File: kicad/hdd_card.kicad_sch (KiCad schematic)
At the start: 17 parts, among them J1 POISK, J2 Conn_01x06, J3 Conn_01x06, U1 28C256, U2 74LS245, U3 28C256, U4 PIC18F47Q10-xP, U5 74LS38, U6 74LS32, U7 74LS74

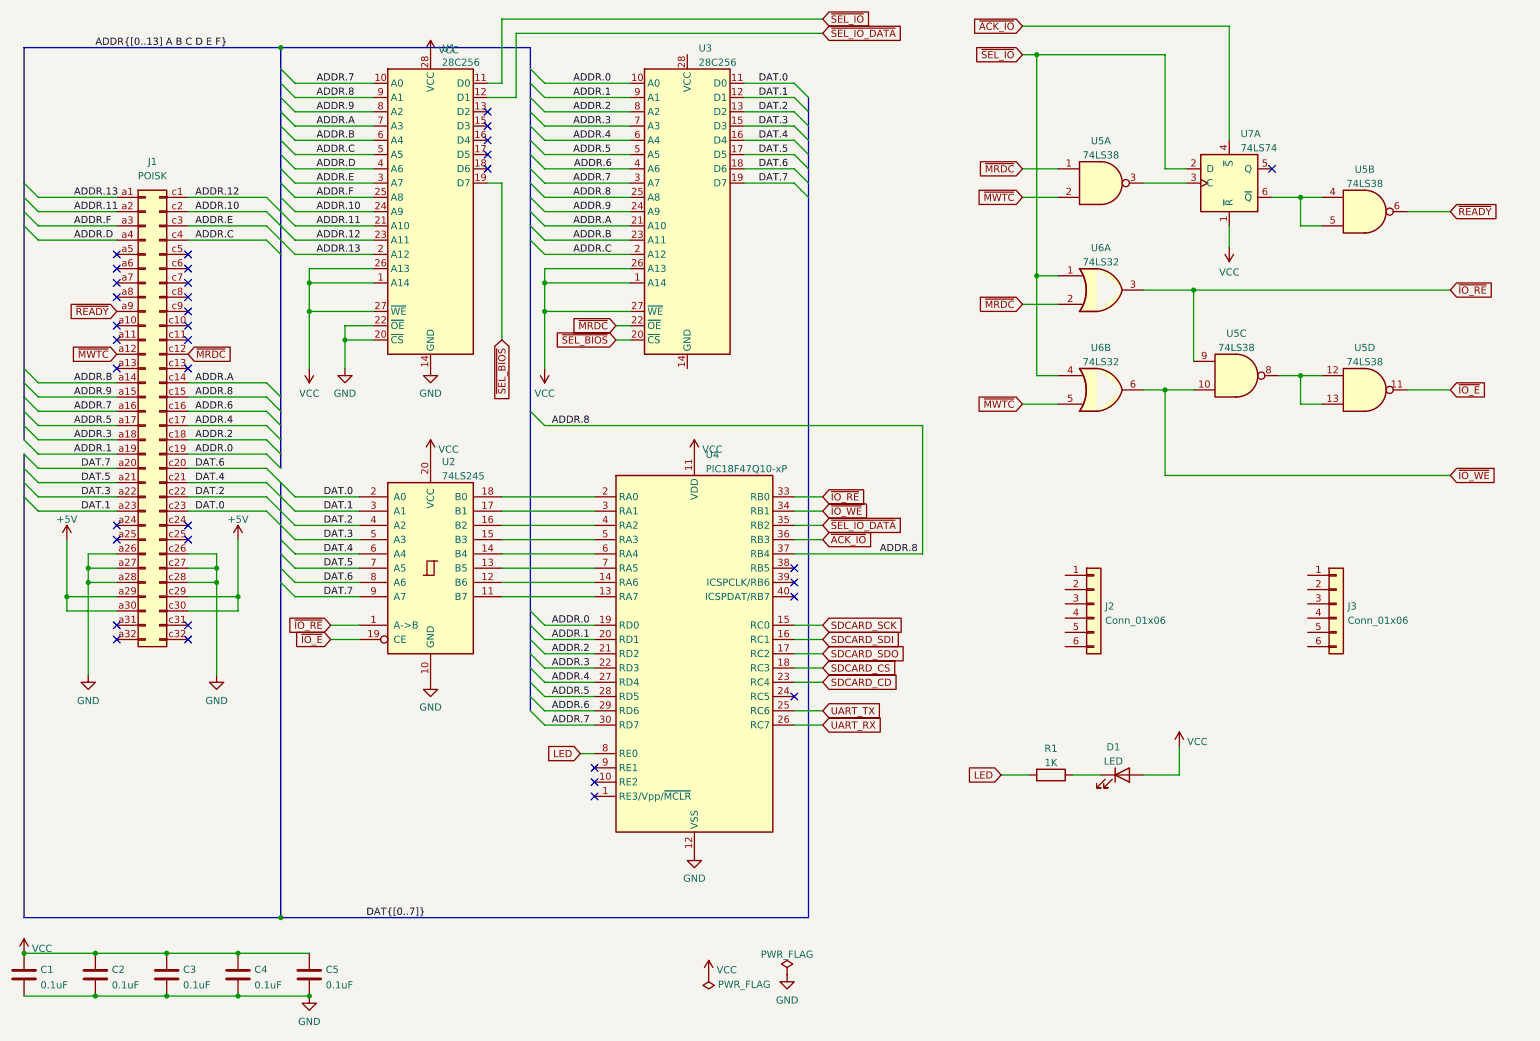
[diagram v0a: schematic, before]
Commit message: Connectors in schematic
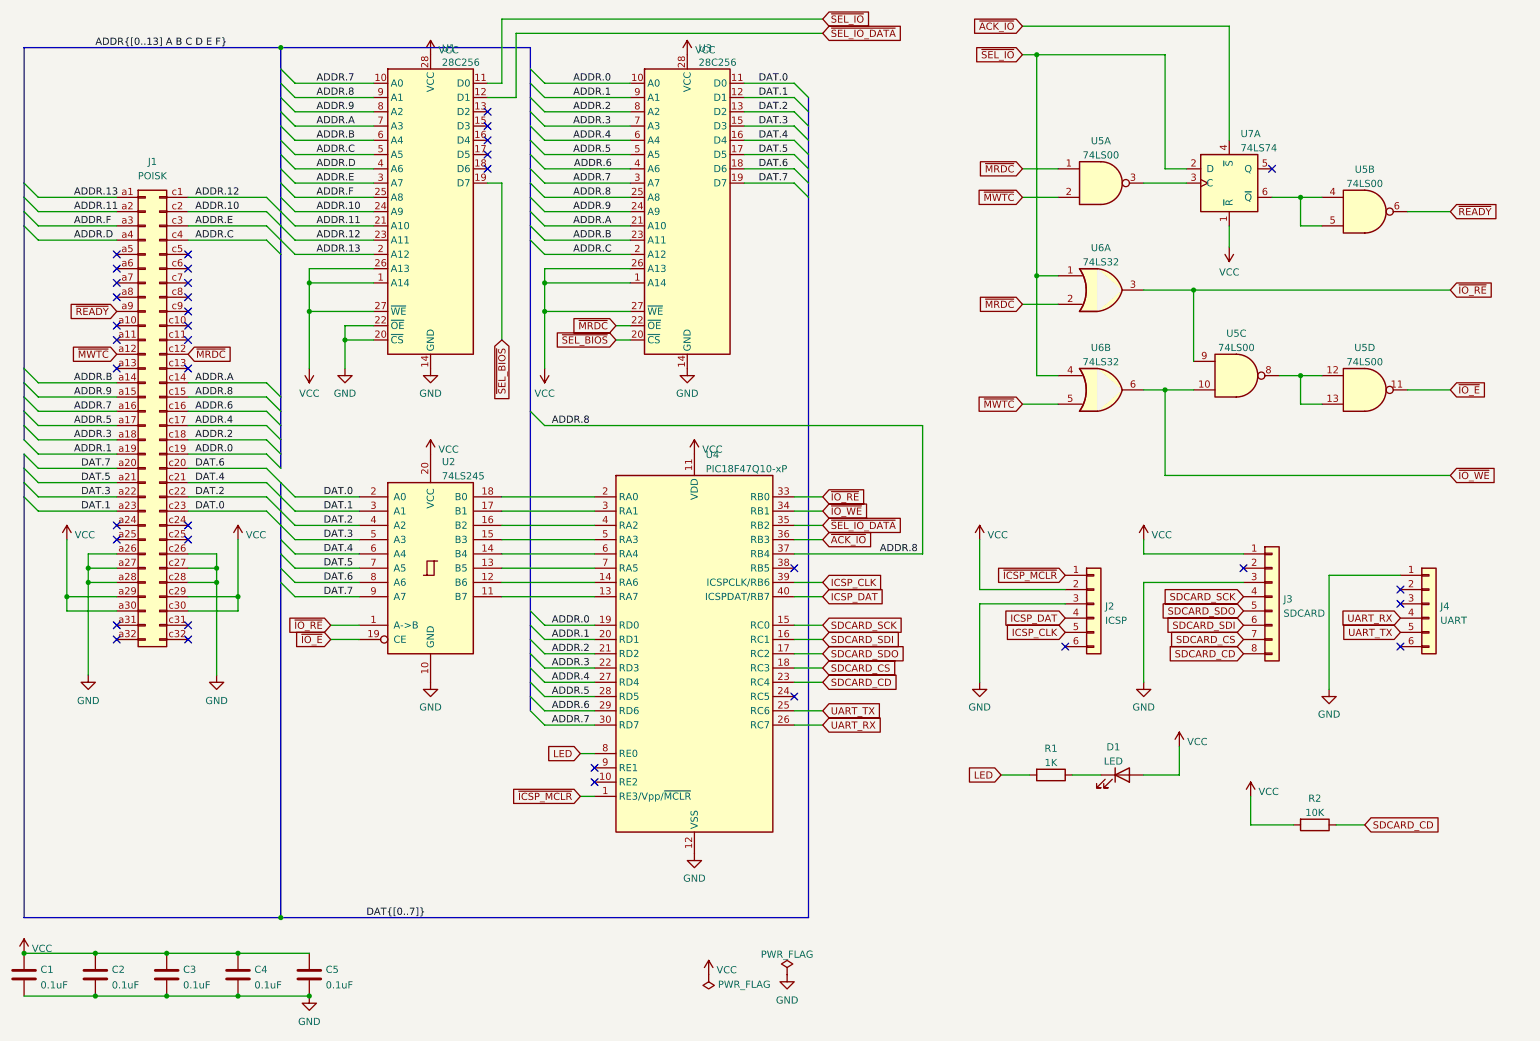
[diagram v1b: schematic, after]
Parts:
- removed U5: 74LS38, symbol 74xx:74LS38
- added J4: UART, symbol Connector_Generic:Conn_01x06
- added R2: 10K, symbol Device:R
- added U5: 74LS00, symbol 74xx:74LS00
- J2: value Conn_01x06 -> ICSP
- J3: value Conn_01x06 -> SDCARD; symbol Connector_Generic:Conn_01x06 -> Connector_Generic:Conn_01x08
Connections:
- net +5V is gone; now on net VCC: J1.a29 (Pin_a29), J1.a30 (Pin_a30), J1.c29 (Pin_c29), J1.c30 (Pin_c30)
- net GND: now also J2.3 (Pin_3), J3.3 (Pin_3), U3.14 (GND), J4.1 (Pin_1)
- net SDCARD_CD: now also J3.8 (Pin_8), R2.1
- net SDCARD_CS: now also J3.7 (Pin_7)
- net SDCARD_SCK: now also J3.4 (Pin_4)
- net SDCARD_SDI: now also J3.6 (Pin_6)
- net SDCARD_SDO: now also J3.5 (Pin_5)
- net UART_RX: now also J4.4 (Pin_4)
- net UART_TX: now also J4.5 (Pin_5)
- net VCC: now also J2.2 (Pin_2), J3.1 (Pin_1), U3.28 (VCC), R2.2
- net ~{IO_E}: now also U5.11
- net ~{IO_RE}: now also U5.9
- net ~{IO_WE}: now also U5.10
- net ~{MRDC}: now also U5.1
- net ~{MWTC}: now also U5.2
- net ~{READY}: now also U5.6
- net ~{ICSP_MCLR}: now reaches U4.1 (RE3/Vpp/~{MCLR})
- net ~{ICSP_MCLR}: now also J2.1 (Pin_1)
- net ICSP_CLK: now reaches U4.39 (ICSPCLK/RB6)
- net ICSP_CLK: now also J2.5 (Pin_5)
- net ICSP_DAT: now reaches U4.40 (ICSPDAT/RB7)
- net ICSP_DAT: now also J2.4 (Pin_4)
- net at U7.3 (C): now also U5.3
- net at U7.6 (~{Q}): now also U5.4, U5.5
- new net: U5.12, U5.13, U5.8
- no-connect marks 36 -> 38

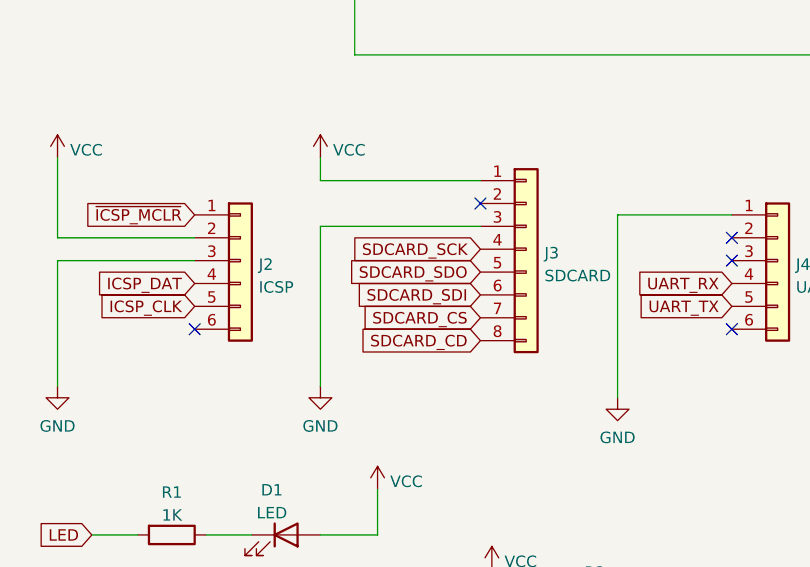
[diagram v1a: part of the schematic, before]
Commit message: Fix SDCARD pinout
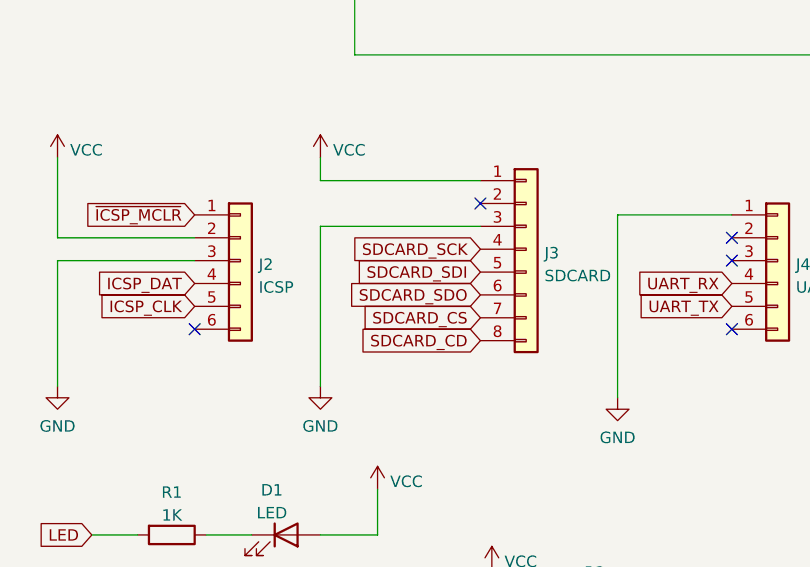
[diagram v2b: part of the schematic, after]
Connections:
- net SDCARD_SDI: now also J3.5 (Pin_5); no longer J3.6 (Pin_6)
- net SDCARD_SDO: now also J3.6 (Pin_6); no longer J3.5 (Pin_5)
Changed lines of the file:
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@@
     )
   )
-  (global_label "SDCARD_SDI" (shape input) (at 234.95 125.73 180) (fields_autoplaced)
+  (global_label "SDCARD_SDI" (shape input) (at 234.95 123.19 180) (fields_autoplaced)
     (effects (font (size 1.27 1.27)) (justify right))
-    (property "Intersheet References" "${INTERSHEET_REFS}" (id 0) (at 221.1069 125.8094 0)
+    (property "Intersheet References" "${INTERSHEET_REFS}" (id 0) (at 221.1069 123.2694 0)
       (effects (font (size 1.27 1.27)) (justify right) hide)
     )
@@
     )
   )
-  (global_label "SDCARD_SDO" (shape input) (at 234.95 123.19 180) (fields_autoplaced)
+  (global_label "SDCARD_SDO" (shape input) (at 234.95 125.73 180) (fields_autoplaced)
     (effects (font (size 1.27 1.27)) (justify right))
-    (property "Intersheet References" "${INTERSHEET_REFS}" (id 0) (at 220.3812 123.2694 0)
+    (property "Intersheet References" "${INTERSHEET_REFS}" (id 0) (at 220.3812 125.8094 0)
       (effects (font (size 1.27 1.27)) (justify right) hide)
     )

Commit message: 4K IO aperture
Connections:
- net ADDR.8: now also U4.35 (RB2); no longer U4.37 (RB4)
- net ADDR.9: now also U4.36 (RB3)
- net ADDR.A: now also U4.37 (RB4)
- net ADDR.B: now also U4.38 (RB5)
- net ~{ACK_IO}: now also U4.24 (RC5); no longer U4.36 (RB3)
- net ~{SEL_IO_DATA}: no longer names the net of U1.12 (D1)
- net ~{SEL_IO_DATA}: no longer U4.35 (RB2)
- no-connect marks 38 -> 37

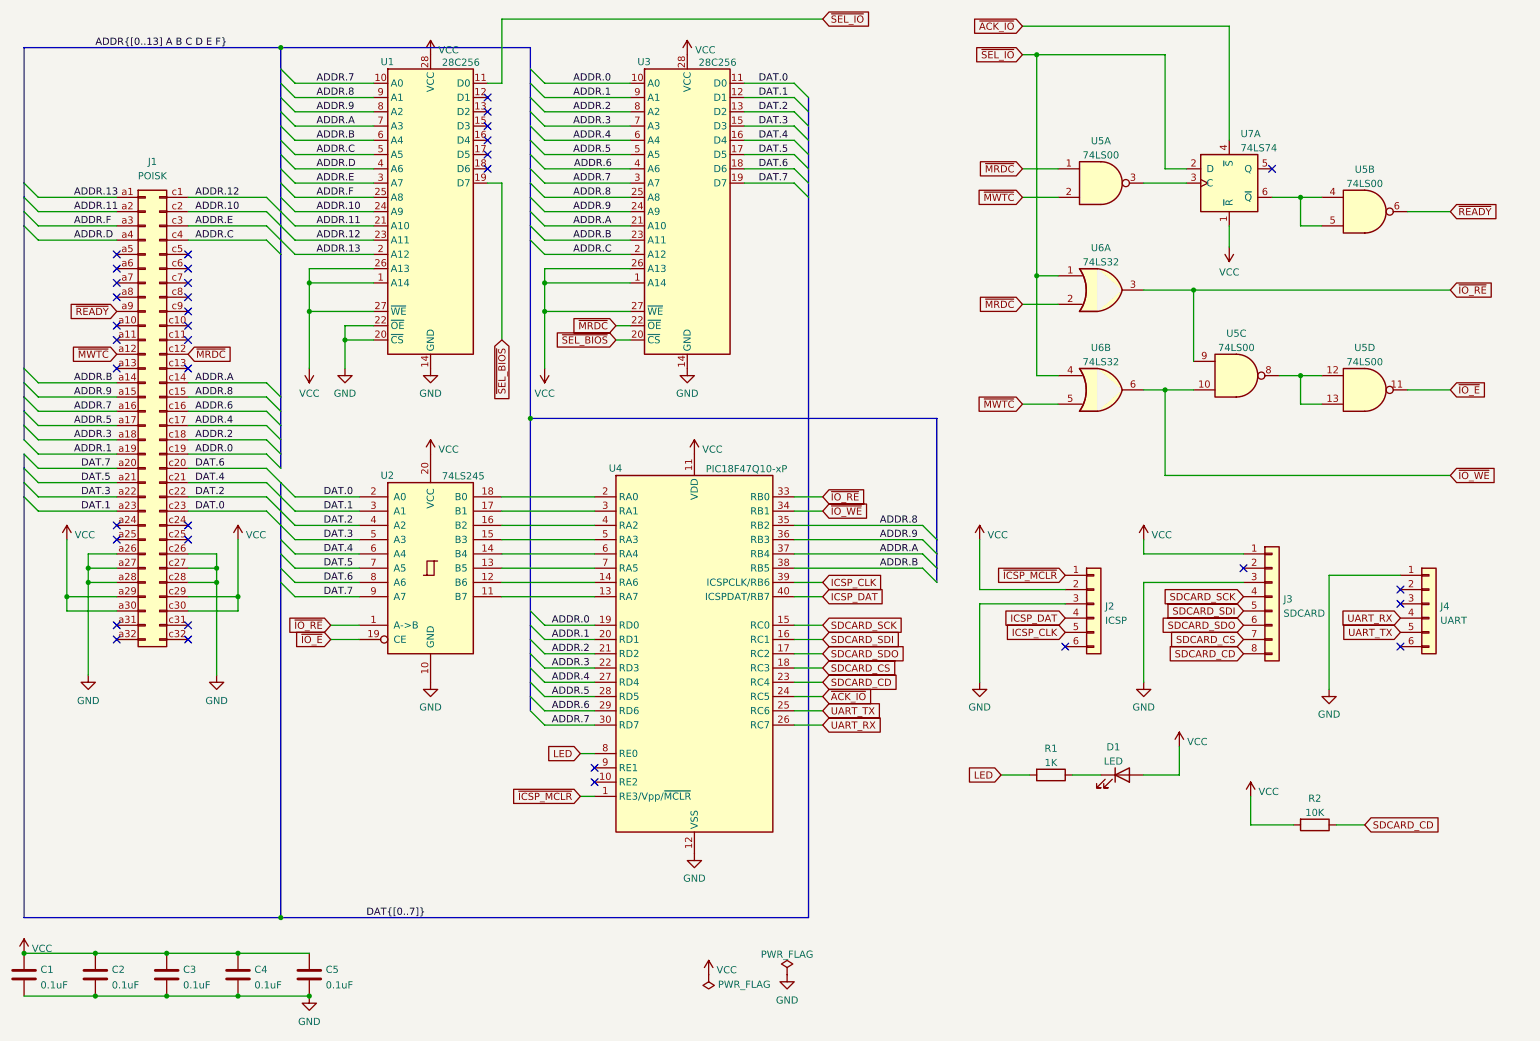
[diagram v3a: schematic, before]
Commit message: Configurable memory mapping to 128 byte blocks
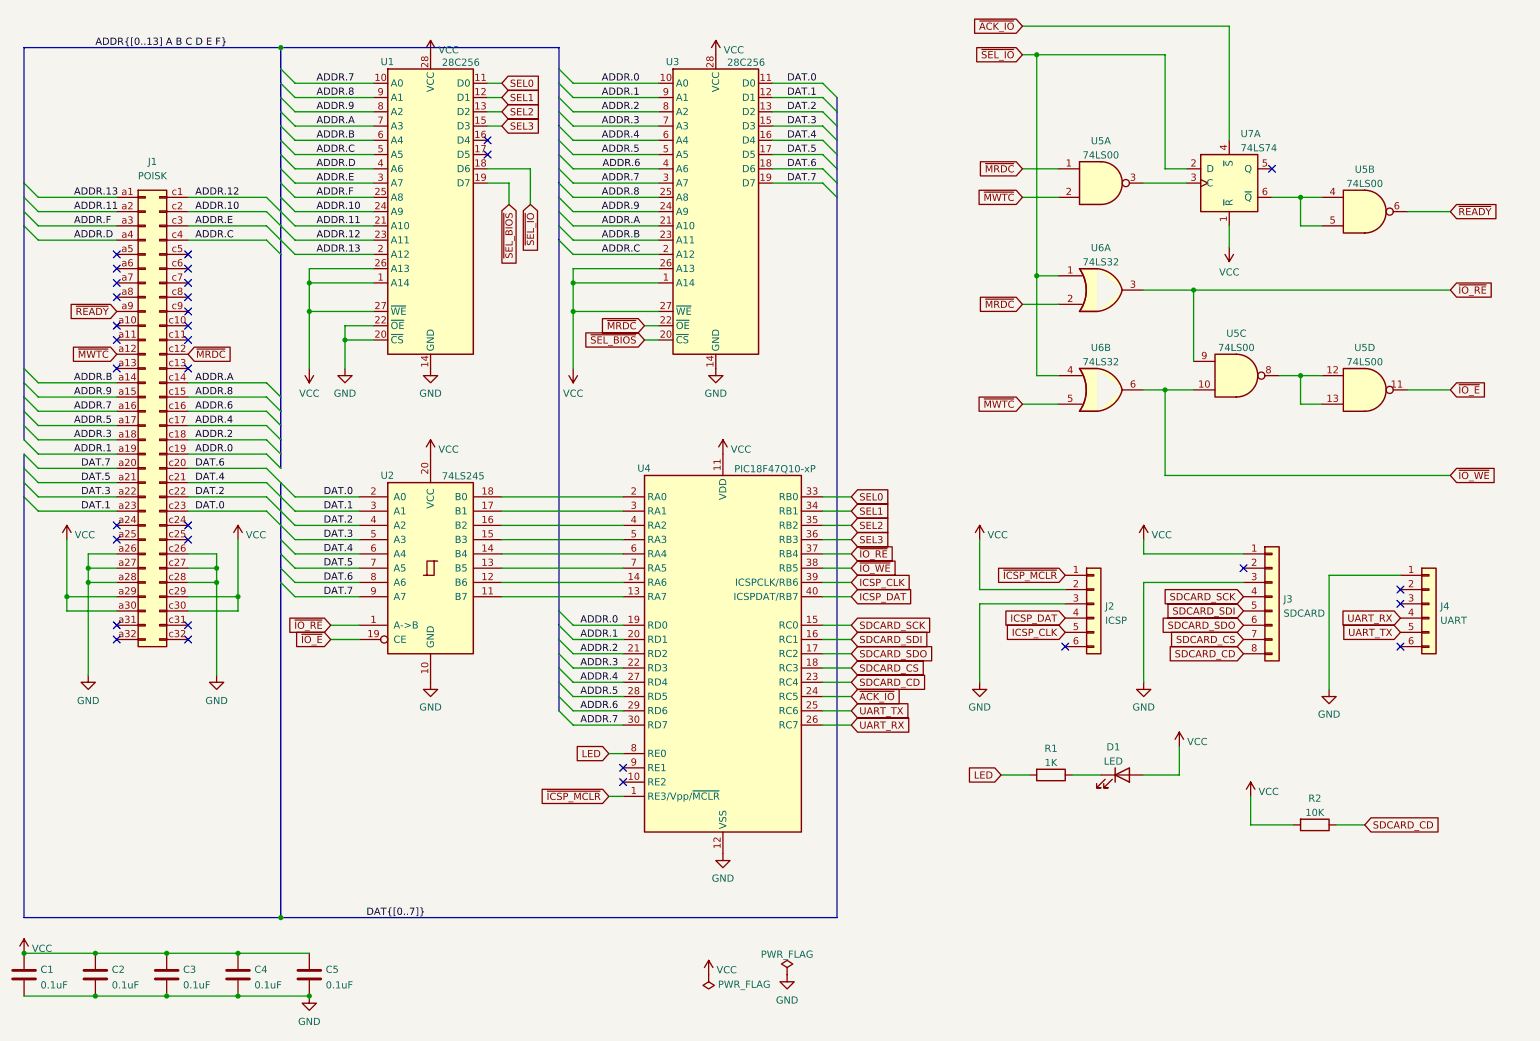
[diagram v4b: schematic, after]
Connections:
- net ADDR.8: no longer U4.35 (RB2)
- net ADDR.9: no longer U4.36 (RB3)
- net ADDR.A: no longer U4.37 (RB4)
- net ADDR.B: no longer U4.38 (RB5)
- net ~{IO_RE}: now also U4.37 (RB4); no longer U4.33 (RB0)
- net ~{IO_WE}: now also U4.38 (RB5); no longer U4.34 (RB1)
- net ~{SEL_IO}: now also U1.18 (D6); no longer U1.11 (D0)
- net SEL1: now reaches U1.12 (D1)
- net SEL1: now also U4.34 (RB1)
- net SEL2: now reaches U1.13 (D2)
- net SEL2: now also U4.35 (RB2)
- net SEL3: now reaches U1.15 (D3)
- net SEL3: now also U4.36 (RB3)
- new net SEL0: U1.11 (D0), U4.33 (RB0)
- no-connect marks 37 -> 33
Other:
- moved on the sheet: U3, U4

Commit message: Check adapter before installing the int13h handler
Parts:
- removed unit 2 of U5
- added C6: 0.1uF, Capacitor_THT:C_Disc_D3.0mm_W1.6mm_P2.50mm, symbol Device:C
- added R3, R4: 10K, symbol Device:R
- added U8: 74LS05, symbol 74xx:74LS05
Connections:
- net GND: now also C6.2
- net SDCARD_CD: now also R4.1; no longer R2.1
- net VCC: now also R2.1, R3.2, R4.2; no longer R2.2
- net ~{ICSP_MCLR}: now also C6.1
- net ~{READY}: now also R2.2, U8.2
- net at U7.6 (~{Q}): now also U8.1
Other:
- moved on the sheet: R2

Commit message: Support formatting floppies
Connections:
- net ~{ICSP_MCLR}: now also R3.1
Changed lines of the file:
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@@
     )
   )
-  (global_label "~{ICSP_MCLR}" (shape output) (at 269.24 152.4 180) (fields_autoplaced)
-    (effects (font (size 1.27 1.27)) (justify right))
-    (property "Intersheet References" "${INTERSHEET_REFS}" (id 0) (at 256.4855 152.3206 0)
-      (effects (font (size 1.27 1.27)) (justify right) hide)
+  (global_label "~{ICSP_MCLR}" (shape output) (at 256.54 152.4 0) (fields_autoplaced)
+    (effects (font (size 1.27 1.27)) (justify left))
+    (property "Intersheet References" "${INTERSHEET_REFS}" (id 0) (at 269.2945 152.4794 0)
+      (effects (font (size 1.27 1.27)) (justify left) hide)
     )
   )
@@
     )
   )
-  (global_label "SDCARD_CD" (shape input) (at 256.54 161.29 0) (fields_autoplaced)
+  (global_label "SDCARD_CD" (shape output) (at 256.54 161.29 0) (fields_autoplaced)
     (effects (font (size 1.27 1.27)) (justify left))
     (property "Intersheet References" "${INTERSHEET_REFS}" (id 0) (at 269.8388 161.2106 0)
